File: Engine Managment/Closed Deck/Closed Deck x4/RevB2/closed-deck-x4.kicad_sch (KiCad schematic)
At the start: 0 parts

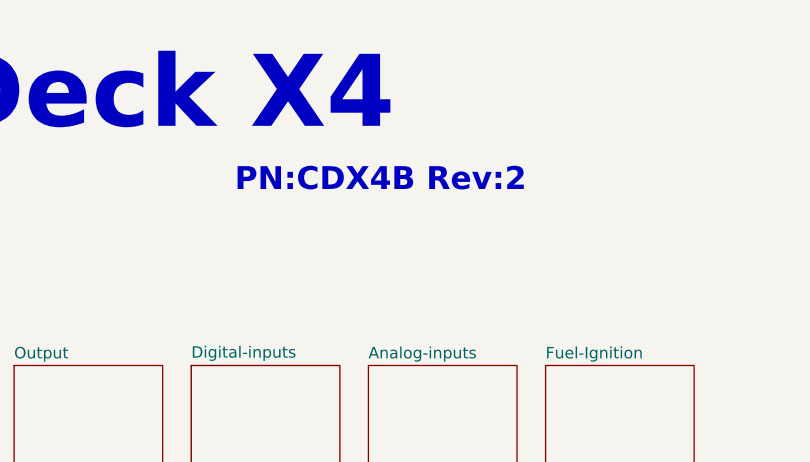
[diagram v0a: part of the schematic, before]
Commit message: Incorrect version cdx4 previously uploaded
Remove cdx4 rev3 (unreleased beta) / Replace cdx4 rev2 with correct version
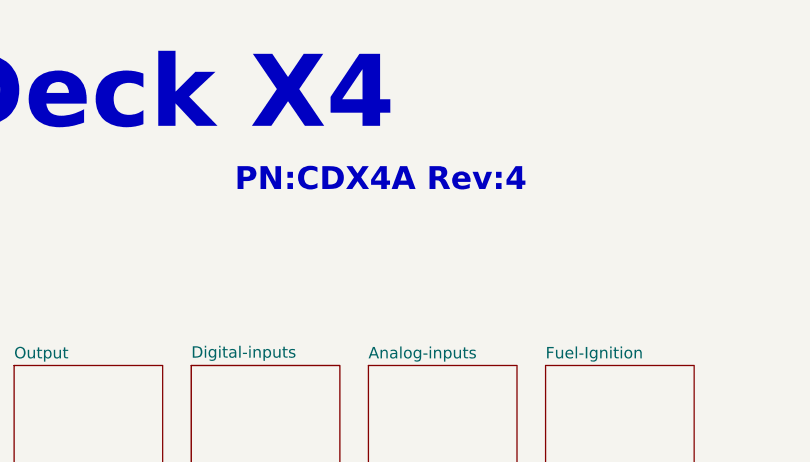
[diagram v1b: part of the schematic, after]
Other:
- note added: "PN:CDX4A Rev:4"
- note removed: "PN:CDX4B Rev:2"
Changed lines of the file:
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@@
 	(title_block
 		(title "Closed Deck X4")
-		(date "2026-05-06")
-		(rev "B2")
+		(date "2026-01-03")
+		(rev "4")
 		(company "OpenLogicEFI")
 		(comment 1 "openlogicefi.com")
@@
 		)
 	)
-	(text "PN:CDX4B Rev:2"
+	(text "PN:CDX4A Rev:4"
 		(exclude_from_sim no)
 		(at 169.926 82.55 0)
@@
 			(project "closed-deck-x4"
 				(path "/929a9b03-e99e-4b88-8e16-759f8c6b59a5"
-					(page "1")
-				)
-			)
+					(page "9")
+				)
+			)
